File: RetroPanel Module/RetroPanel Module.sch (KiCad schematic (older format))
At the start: 17 parts, among them J1 Front Panel, M1 Mounting_Pin, M10 Mounting_Pad, M11 Mounting_Pad, M12 Mounting_Pad, M13 Mounting_Pad, M14 Mounting_Pad, M15 Mounting_Pad, M16 Mounting_Pin, M2 Mounting_Pin, M3 Mounting_Pin, M4 Mounting_Pad, M5 Mounting_Pad, M6 Mounting_Pad, M7 Mounting_Pad, M8 Mounting_Pad, M9 Mounting_Pad

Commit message: First schematic draft
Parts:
- added A1: Arduino_Pro_Micro, arduino_pro_micro:Arduino_Pro_Micro, symbol arduino_pro_micro:Arduino_Pro_Micro
- added C4, C6, C7, C8, C9: 100nF, Capacitor_THT:C_Disc_D4.7mm_W2.5mm_P5.00mm, symbol Device:C_Small
- added D1: 1N4001, Diode_THT:D_DO-41_SOD81_P10.16mm_Horizontal, symbol Diode:1N4001
- added J10: SW_EXTRA, Connector_PinHeader_2.54mm:PinHeader_1x02_P2.54mm_Vertical, symbol Connector_Generic:Conn_01x02
- added J11: RS-232, Connector_IDC:IDC-Header_2x05_P2.54mm_Vertical, symbol rs232_conn:RS232
- added J2: SW_POWER, Connector_PinHeader_2.54mm:PinHeader_1x02_P2.54mm_Vertical, symbol Connector_Generic:Conn_01x02
- added J3: LED_POWER, Connector_PinHeader_2.54mm:PinHeader_1x02_P2.54mm_Vertical, symbol Connector_Generic:Conn_01x02
- added J4: SW_RESET, Connector_PinHeader_2.54mm:PinHeader_1x02_P2.54mm_Vertical, symbol Connector_Generic:Conn_01x02
- added J5: SW_TURBO, Connector_PinHeader_2.54mm:PinHeader_1x02_P2.54mm_Vertical, symbol Connector_Generic:Conn_01x02
- added J6: LED_TURBO, Connector_PinHeader_2.54mm:PinHeader_1x02_P2.54mm_Vertical, symbol Connector_Generic:Conn_01x02
- added J7: POWER, pwr_drv:PWR_IN, symbol floppy:Power_Input
- added J8: IIC, Connector_PinHeader_2.54mm:PinHeader_1x04_P2.54mm_Vertical, symbol Connector_Generic:Conn_01x04
- added J9: POST_CARD, Connector_IDC:IDC-Header_2x10_P2.54mm_Vertical, symbol post_card:POST_CARD
- added JP1: ARD_PWR1, solder_bridge:select, symbol solder_select:SolderJumper_3_Bridged12
- added JP2: ARD_PWR2, solder_bridge:select, symbol solder_select:SolderJumper_3_Bridged12
- added Q1, Q2, Q3, Q4: 2N3904, Package_TO_SOT_THT:TO-92_Inline, symbol Transistor_BJT:2N3904
- added R1, R2: 4k7, resistor:R_Axial_DIN0207_L6.3mm_D2.5mm_P10.16mm_Horizontal, symbol Device:R_Small
- added R10, R11, R12, R4, R5, R6, R7, R8, R9: 470, resistor:R_Axial_DIN0207_L6.3mm_D2.5mm_P10.16mm_Horizontal, symbol Device:R_Small
- added R13, R14, R15, R16: 10k, resistor:R_Axial_DIN0207_L6.3mm_D2.5mm_P10.16mm_Horizontal, symbol Device:R_Small
- added R3: 0, resistor:R_Axial_DIN0207_L6.3mm_D2.5mm_P10.16mm_Horizontal, symbol Device:R_Small
- added U1: LM35-LP, Package_TO_SOT_THT:TO-92_Inline_Wide, symbol Sensor_Temperature:LM35-LP
- added U4: MAX232A, Package_DIP:DIP-16_W7.62mm_Socket_LongPads, symbol Interface_UART:MAX232
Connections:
- net labels added: +5V, ARD_PWR, DIG1, DIG2, DIG3, DIG4, IIC_SCL, IIC_SDA, RS232_RX, RS232_TX, TEMP, TTL_RX, TTL_TX
- net labels removed: VCC
- wire segments 62 -> 223
- no-connect marks 0 -> 9
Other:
- moved on the sheet: J1

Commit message: First layout draft done
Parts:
- removed C4, C6, C7, C8, C9: 100nF, Capacitor_THT:C_Disc_D4.7mm_W2.5mm_P5.00mm, symbol Device:C_Small
- removed J11: RS-232, Connector_IDC:IDC-Header_2x05_P2.54mm_Vertical, symbol rs232_conn:RS232
- removed U1: LM35-LP, Package_TO_SOT_THT:TO-92_Inline_Wide, symbol Sensor_Temperature:LM35-LP
- removed U4: MAX232A, Package_DIP:DIP-16_W7.62mm_Socket_LongPads, symbol Interface_UART:MAX232
- added J16: SPEAKER, RetroPanel:PinHeader_1x04_P2.54mm_Vertical, symbol Connector_Generic:Conn_01x04
- added JP3: TURBO_SEL, solder_bridge:select, symbol solder_select:SolderJumper_3_Bridged12
- added JP4: LED_VCC, solder_bridge:select, symbol solder_select:SolderJumper_3_Bridged12
- added JP5: 7S_TYPE, solder_bridge:select, symbol solder_select:SolderJumper_3_Bridged12
- added LS1: Speaker, Buzzer_Beeper:Buzzer_12x9.5RM7.6, symbol Device:Speaker
- added R17: 0, resistor:R_Axial_DIN0207_L6.3mm_D2.5mm_P10.16mm_Horizontal, symbol Device:R_Small
- J10, J2, J3, J4, J5, J6: footprint Connector_PinHeader_2.54mm:PinHeader_1x02_P2.54mm_Vertical -> RetroPanel:PinHeader_1x02_P2.54mm_Vertical
- J7: footprint pwr_drv:PWR_IN -> RetroPanel:Molex_KK-254_1x04_P2.54mm_Horizontal
- JP1: value ARD_PWR1 -> LED_PWR1
- JP2: value ARD_PWR2 -> LED_PWR2
- Q1, Q2, Q3, Q4: footprint Package_TO_SOT_THT:TO-92_Inline -> Package_TO_SOT_THT:TO-92_Inline_Wide
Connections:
- net +5V: now also JP4.3 (B), JP5.3 (B)
- net ARD_PWR: now also JP4.1 (A); no longer R4.1
- net GND: now also JP5.1 (A); no longer Q1.1 (E), Q2.1 (E), Q3.1 (E), Q4.1 (E)
- net LED_TURBO1: now also JP3.3 (B)
- net SW_TURBO1: now also JP3.1 (A)
- net at J3.1 (Pin_1): now also R17.2; no longer JP1.1 (A)
- net TEMP: no longer names the net of A1.20 (D21)
- net TEMP: now also JP3.2 (C)
- new net: JP5.2 (C), Q1.1 (E), Q2.1 (E), Q3.1 (E), Q4.1 (E)
- new net: J16.1 (Pin_1), LS1.1
- new net: J16.4 (Pin_4), LS1.2
- new net: JP1.1 (A), R17.1
- new net: JP4.2 (C), R4.1
- no-connect marks 9 -> 6
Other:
- note added: "Can connect a diagnostic card - OR - install\nArduino for controlling 7 segment display."
- note added: "Determines if 7 segment display is CA or\nCK - link 1-2 for CK display. When using\nCA-display, install Q1-Q4 backwards."
- note added: "Power LED, can have it coming in from the system\nvia J3, controlled by Arduino linking LED_PWR1-2\nacross pins 2-3. Link LED_VCC 1-2, if skipping\nArduino then link 2-3 to wire to VCC directly."
- note added: "Some pentium-era machines only have\nLED, but no switch so we may need to\nread voltage going to LED. If using switch,\nflip cable if mode seems "stuck"."
- moved on the sheet: D1, J1, J10, J2, J3, J4, J5, J6, J7, J8, JP1, JP2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

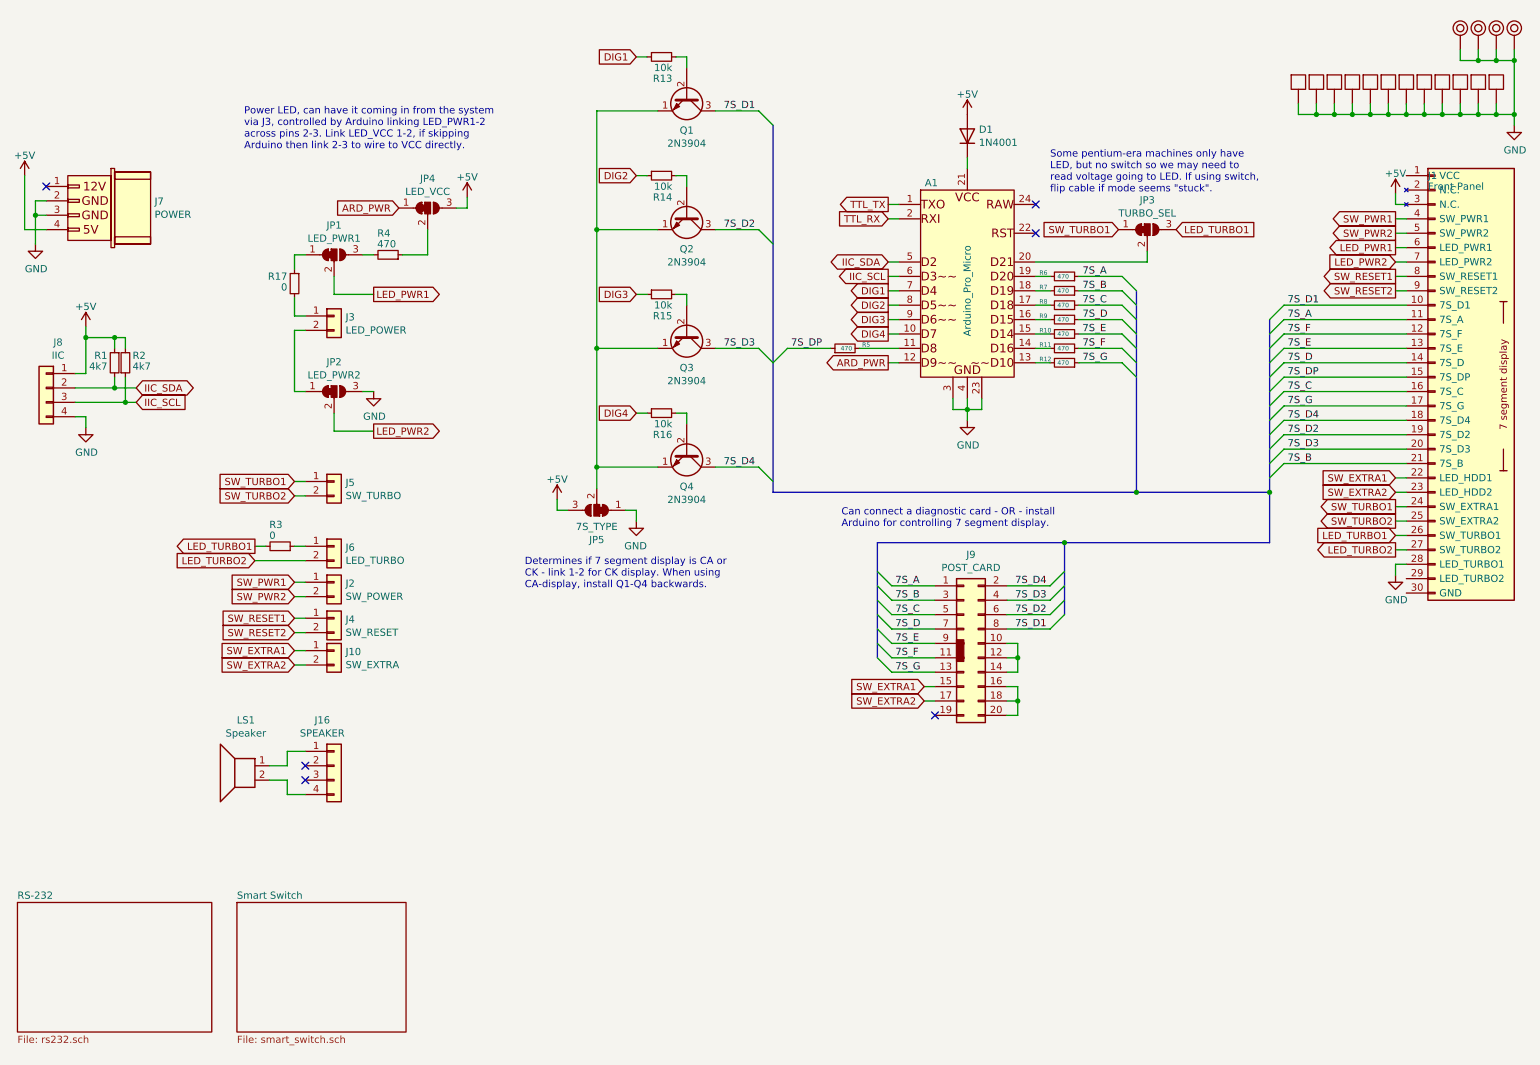
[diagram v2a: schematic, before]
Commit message: Faceplate FP1 and HDD LED
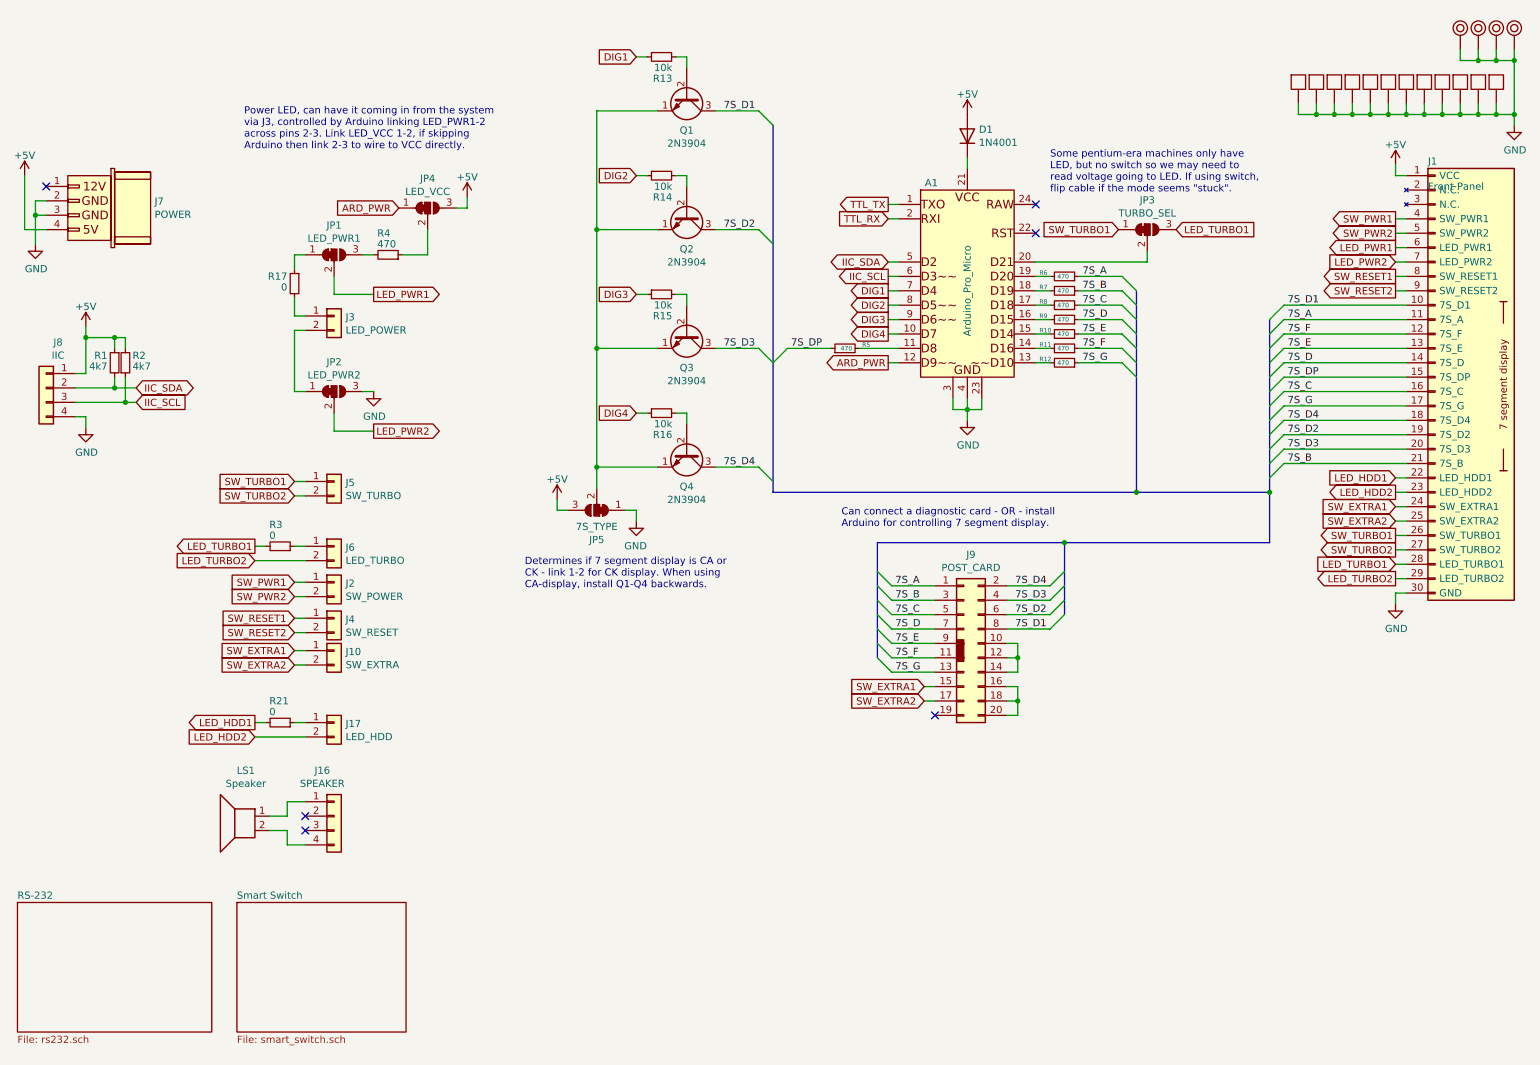
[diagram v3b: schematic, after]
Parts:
- added J17: LED_HDD, RetroPanel:PinHeader_1x02_P2.54mm_Vertical, symbol Connector_Generic:Conn_01x02
- added R21: 0, resistor:R_Axial_DIN0207_L6.3mm_D2.5mm_P10.16mm_Horizontal, symbol Device:R_Small
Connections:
- net +5V: now also J1.1 (VCC); no longer J1.3 (N.C.)
- net GND: now also J1.30 (GND); no longer J1.28 (LED_TURBO1)
- net LED_TURBO1: now also J1.28 (LED_TURBO1); no longer J1.26 (SW_TURBO1)
- net LED_TURBO2: now also J1.29 (LED_TURBO2); no longer J1.27 (SW_TURBO2)
- net SW_EXTRA1: now also J1.24 (SW_EXTRA1); no longer J1.22 (LED_HDD1)
- net SW_EXTRA2: now also J1.25 (SW_EXTRA2); no longer J1.23 (LED_HDD2)
- net SW_TURBO1: now also J1.26 (SW_TURBO1); no longer J1.24 (SW_EXTRA1)
- net SW_TURBO2: now also J1.27 (SW_TURBO2); no longer J1.25 (SW_EXTRA2)
- new net: J17.1 (Pin_1), R21.1
- new net LED_HDD1: J1.22 (LED_HDD1), R21.2
- new net LED_HDD2: J1.23 (LED_HDD2), J17.2 (Pin_2)
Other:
- note added: "Some pentium-era machines only have\nLED, but no switch so we may need to\nread voltage going to LED. If using switch,\nflip cable if the mode seems "stuck"."
- note removed: "Some pentium-era machines only have\nLED, but no switch so we may need to\nread voltage going to LED. If using switch,\nflip cable if mode seems "stuck"."
- moved on the sheet: J16, LS1
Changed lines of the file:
@@
 U 1 1 62825997
 P 10525 2850
-F 0 "J1" H 10475 4050 50  0000 L CNN
+F 0 "J1" H 10475 4150 50  0000 L CNN
 F 1 "Front Panel" H 10475 3975 50  0000 L CNN
 F 2 "RetroPanel:Module_Panel" H 10525 2850 50  0001 C CNN
@@
 L power:GND #PWR0101
 U 1 1 6282785A
-P 10250 4425
-F 0 "#PWR0101" H 10250 4175 50  0001 C CNN
-F 1 "GND" H 10255 4252 50  0000 C CNN
-F 2 "" H 10250 4425 50  0001 C CNN
-F 3 "" H 10250 4425 50  0001 C CNN
-	1    10250 4425
-	1    0    0    -1
-$EndComp
-Wire Wire Line
-	10325 4350 10250 4350
-Wire Wire Line
-	10250 1775 10250 1850
-Wire Wire Line
-	10250 1850 10325 1850
-Wire Wire Line
-	10250 4350 10250 4425
+P 10250 4625
+F 0 "#PWR0101" H 10250 4375 50  0001 C CNN
+F 1 "GND" H 10255 4452 50  0000 C CNN
+F 2 "" H 10250 4625 50  0001 C CNN
+F 3 "" H 10250 4625 50  0001 C CNN
+	1    10250 4625
+	1    0    0    -1
+$EndComp
+Wire Wire Line
+	10325 4550 10250 4550
+Wire Wire Line
+	10250 1575 10250 1650
+Wire Wire Line
+	10250 1650 10325 1650
+Wire Wire Line
+	10250 4550 10250 4625
 Text GLabel 10250 1950 0    50   Output ~ 0
 SW_PWR1
@@
 Text GLabel 10250 2250 0    50   Input ~ 0
 LED_PWR2
-Text GLabel 10250 3950 0    50   Output ~ 0
+Text GLabel 10250 4150 0    50   Output ~ 0
 SW_TURBO1
-Text GLabel 10250 4050 0    50   Output ~ 0
+Text GLabel 10250 4250 0    50   Output ~ 0
 SW_TURBO2
-Text GLabel 10250 4150 0    50   Input ~ 0
+Text GLabel 10250 4350 0    50   Input ~ 0
 LED_TURBO1
-Text GLabel 10250 4250 0    50   Output ~ 0
+Text GLabel 10250 4450 0    50   Output ~ 0
 LED_TURBO2
 Text GLabel 10250 2350 0    50   Output ~ 0
@@
 	10250 2450 10325 2450
 Wire Wire Line
-	10250 3950 10325 3950
-Wire Wire Line
-	10250 4050 10325 4050
-Wire Wire Line
 	10250 4150 10325 4150
 Wire Wire Line
 	10250 4250 10325 4250
+Wire Wire Line
+	10250 4350 10325 4350
+Wire Wire Line
+	10250 4450 10325 4450
 Wire Wire Line
 	9475 2550 10325 2550
@@
 Text Label 9500 2850 0    50   ~ 0
 7S_E
-Text GLabel 10250 3750 0    50   Input ~ 0
+Text GLabel 10250 3950 0    50   Input ~ 0
 SW_EXTRA1
-Text GLabel 10250 3850 0    50   Input ~ 0
+Text GLabel 10250 4050 0    50   Input ~ 0
 SW_EXTRA2
 Wire Wire Line
-	10250 3750 10325 3750
-Wire Wire Line
-	10250 3850 10325 3850
+	10250 3950 10325 3950
+Wire Wire Line
+	10250 4050 10325 4050
 $Comp
 L mounting:Mounting_Pad M14
@@
 L power:+5V #PWR0103
 U 1 1 6371133E
-P 10250 1775
-F 0 "#PWR0103" H 10250 1625 50  0001 C CNN
-F 1 "+5V" H 10250 1915 50  0000 C CNN
-F 2 "" H 10250 1775 50  0000 C CNN
-F 3 "" H 10250 1775 50  0000 C CNN
-	1    10250 1775
+P 10250 1575
+F 0 "#PWR0103" H 10250 1425 50  0001 C CNN
+F 1 "+5V" H 10250 1715 50  0000 C CNN
+F 2 "" H 10250 1575 50  0000 C CNN
+F 3 "" H 10250 1575 50  0000 C CNN
+	1    10250 1575
 	1    0    0    -1
 $EndComp
@@
 	8525 2175 8525 2250
 Text Notes 7850 1775 0    50   ~ 0
-Some pentium-era machines only have\nLED, but no switch so we may need to\nread voltage going to LED. If using switch,\nflip cable if mode seems "stuck".
+Some pentium-era machines only have\nLED, but no switch so we may need to\nread voltage going to LED. If using switch,\nflip cable if the mode seems "stuck".
 Text Notes 6400 4100 0    50   ~ 0
 Can connect a diagnostic card - OR - install\nArduino for controlling 7 segment display.
@@
 L Device:Speaker LS1
 U 1 1 63891002
-P 2225 5750
-F 0 "LS1" H 2188 6067 50  0000 C CNN
-F 1 "Speaker" H 2188 5976 50  0000 C CNN
-F 2 "Buzzer_Beeper:Buzzer_12x9.5RM7.6" H 2225 5550 50  0001 C CNN
-F 3 "~" H 2215 5700 50  0001 C CNN
-	1    2225 5750
+P 2225 6100
+F 0 "LS1" H 2188 6417 50  0000 C CNN
+F 1 "Speaker" H 2188 6326 50  0000 C CNN
+F 2 "Buzzer_Beeper:Buzzer_12x9.5RM7.6" H 2225 5900 50  0001 C CNN
+F 3 "~" H 2215 6050 50  0001 C CNN
+	1    2225 6100
 	-1   0    0    -1
 $EndComp
@@
 L Connector_Generic:Conn_01x04 J16
 U 1 1 63893EDF
-P 2875 5750
-F 0 "J16" H 2793 6067 50  0000 C CNN
-F 1 "SPEAKER" H 2793 5976 50  0000 C CNN
-F 2 "RetroPanel:PinHeader_1x04_P2.54mm_Vertical" H 2875 5750 50  0001 C CNN
-F 3 "~" H 2875 5750 50  0001 C CNN
-	1    2875 5750
-	1    0    0    -1
-$EndComp
-NoConn ~ 2675 5750
-NoConn ~ 2675 5850
-Wire Wire Line
-	2675 5650 2550 5650
-Wire Wire Line
-	2550 5650 2550 5750
-Wire Wire Line
-	2550 5750 2425 5750
-Wire Wire Line
-	2425 5850 2550 5850
-Wire Wire Line
-	2550 5850 2550 5950
-Wire Wire Line
-	2550 5950 2675 5950
+P 2875 6100
+F 0 "J16" H 2793 6417 50  0000 C CNN
+F 1 "SPEAKER" H 2793 6326 50  0000 C CNN
+F 2 "RetroPanel:PinHeader_1x04_P2.54mm_Vertical" H 2875 6100 50  0001 C CNN
+F 3 "~" H 2875 6100 50  0001 C CNN
+	1    2875 6100
+	1    0    0    -1
+$EndComp
+NoConn ~ 2675 6100
+NoConn ~ 2675 6200
+Wire Wire Line
+	2675 6000 2550 6000
+Wire Wire Line
+	2550 6000 2550 6100
+Wire Wire Line
+	2550 6100 2425 6100
+Wire Wire Line
+	2425 6200 2550 6200
+Wire Wire Line
+	2550 6200 2550 6300
+Wire Wire Line
+	2550 6300 2675 6300
 Wire Bus Line
 	9375 3850 9375 4200
+Text GLabel 2325 5450 0    50   Output ~ 0
+LED_HDD1
+Text GLabel 2325 5550 0    50   Input ~ 0
+LED_HDD2
+$Comp
+L Connector_Generic:Conn_01x02 J17
+U 1 1 6365149C
+P 2875 5450
+F 0 "J17" H 2955 5442 50  0000 L CNN
+F 1 "LED_HDD" H 2955 5351 50  0000 L CNN
+F 2 "RetroPanel:PinHeader_1x02_P2.54mm_Vertical" H 2875 5450 50  0001 C CNN
+F 3 "~" H 2875 5450 50  0001 C CNN
+	1    2875 5450
+	1    0    0    -1
+$EndComp
+Wire Wire Line
+	2600 5450 2675 5450
+$Comp
+L Device:R_Small R21
+U 1 1 636514A3
+P 2500 5450
+F 0 "R21" V 2650 5375 50  0000 L CNN
+F 1 "0" V 2575 5375 50  0000 L CNN
+F 2 "resistor:R_Axial_DIN0207_L6.3mm_D2.5mm_P10.16mm_Horizontal" H 2500 5450 50  0001 C CNN
+F 3 "~" H 2500 5450 50  0001 C CNN
+	1    2500 5450
+	0    1    -1   0
+$EndComp
+Wire Wire Line
+	2400 5450 2325 5450
+Wire Wire Line
+	2325 5550 2675 5550
+Text GLabel 10250 3750 0    50   Input ~ 0
+LED_HDD1
+Wire Wire Line
+	10250 3750 10325 3750
+Text GLabel 10250 3850 0    50   Output ~ 0
+LED_HDD2
+Wire Wire Line
+	10250 3850 10325 3850
 Wire Bus Line
 	5925 1300 5925 3850
